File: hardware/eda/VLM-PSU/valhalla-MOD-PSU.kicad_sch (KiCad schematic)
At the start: 31 parts, among them J1 MAINS, J2 DC, J3 BUS, J4 GPIO, Q1 *3, U1 *2

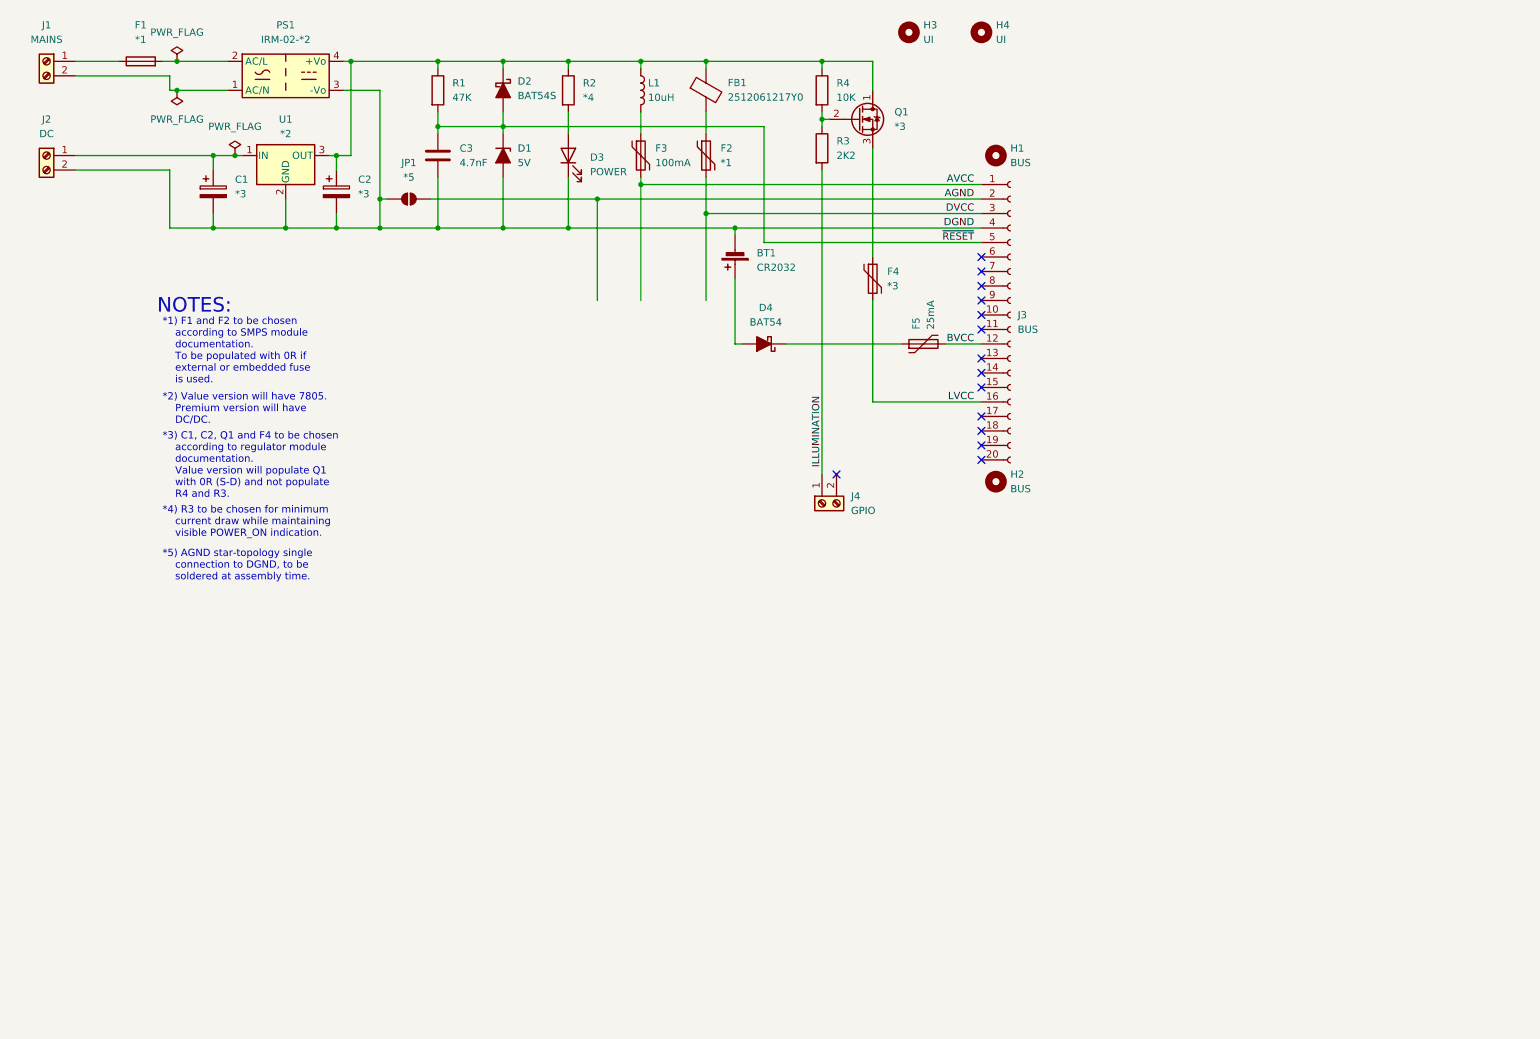
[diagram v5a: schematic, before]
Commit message: UPDATE: started work on MOD-PSU
  - adjusted schematic for cosmetics
  - changed power output to correct part to mate with Molex 5557
  - made /RESET generic (i.e. non-AVR targeted) and moved to a
    GPIO
    - upcoming CPU boards can elect whether to use the PSU-generated
      /RESET or come up with their own implementation
    - premium version will have a supervisor IC generating it,
      value version will have RC delay
  - opted to keep this MOD-PSU as is (i.e. MAINS or DC input) and
    develop a 2nd version for battery operation (UPS)
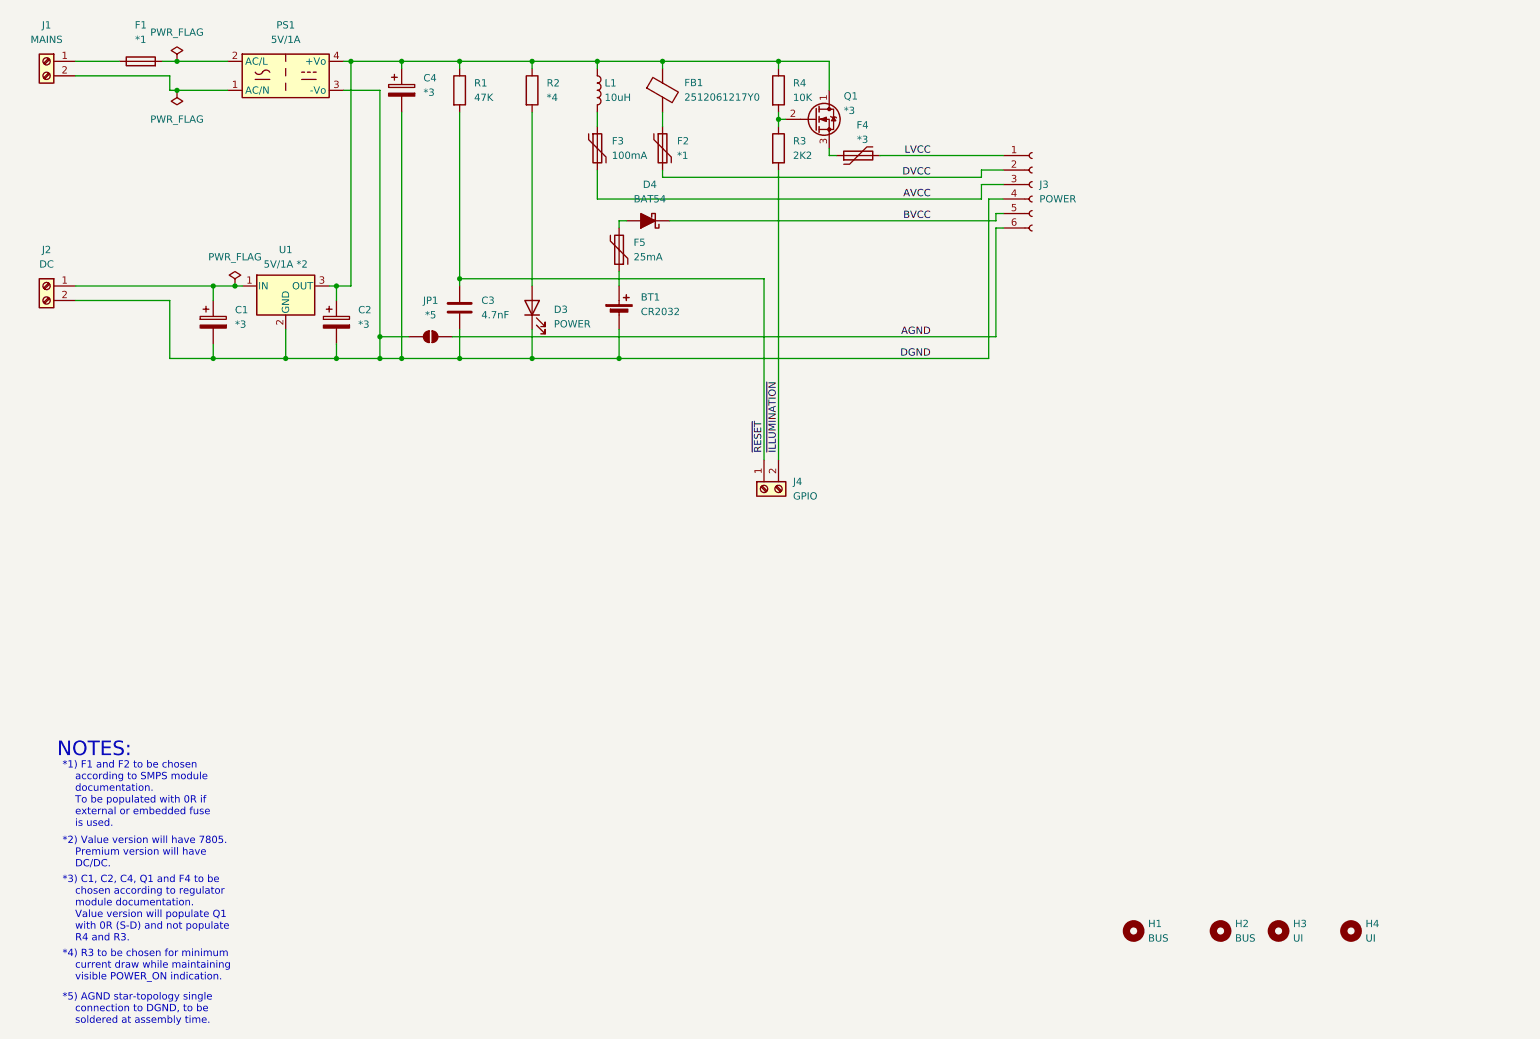
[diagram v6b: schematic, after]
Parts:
- removed D1: 5V, Diode_THT:D_DO-35_SOD27_P7.62mm_Horizontal, symbol Device:D_Zener_Filled
- removed D2: BAT54S, Diode_THT:D_DO-35_SOD27_P7.62mm_Horizontal, symbol Device:D_Schottky_Filled
- removed J3: BUS, Connector_PinSocket_2.54mm:PinSocket_2x10_P2.54mm_Vertical, symbol Connector:Conn_01x20_Socket
- added C4: *3, Capacitor_THT:CP_Radial_D5.0mm_P2.00mm, symbol Device:C_Polarized
- added J3: POWER, symbol Connector:Conn_01x06_Socket
- PS1: value IRM-02-*2 -> 5V/1A
- U1: value *2 -> 5V/1A *2
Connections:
- net AGND: now also J3.6 (Pin_6)
- net AVCC: now also J3.3 (Pin_3)
- net BVCC: now also D4.1 (K), J3.5 (Pin_5); no longer F5.2
- net DGND: now also C4.2, J3.4 (Pin_4)
- net DVCC: now also J3.2 (Pin_2)
- net LVCC: now also J3.1 (Pin_1)
- net ~{RESET}: now also J4.1 (Pin_1)
- net ~{ILLUMINATION}: now reaches J4.2 (Pin_2)
- net ~{ILLUMINATION}: now also R3.2
- net at F5.1: now also BT1.1 (+); no longer D4.1 (K)
- net at C2.1, FB1.1, L1.1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: now also C4.1
- net at D4.2 (A): now also F5.2; no longer BT1.1 (+)
- removed net ILLUMINATION: J4.1 (Pin_1), R3.2
- no-connect marks 14 -> 0
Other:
- note added: "*3) C1, C2, C4, Q1 and F4 to be chosen according to regulator module documentation. Value version will populate Q1 with 0R (S-D) and not populate R4 and R3."
- note removed: "*3) C1, C2, Q1 and F4 to be chosen according to regulator module documentation. Value version will populate Q1 with 0R (S-D) and not populate R4 and R3."
- moved on the sheet: BT1, C1, C2, C3, D3, D4, F2, F3, F4, F5, FB1, H1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

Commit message: UPDATE: progress on MOD-PSU
 - refined the schematic design and started work on the PCB layout
 - selected some critical components, resolved final footprints
   for others
 - found a good compromise for the (initially) /RESET line: using a
   supervisory circuit BUT using it as a POWER_GOOD output. A
   connected CPU can thus choose whether to interpret that as PG
   (early warning) or /RESET (closing shop).
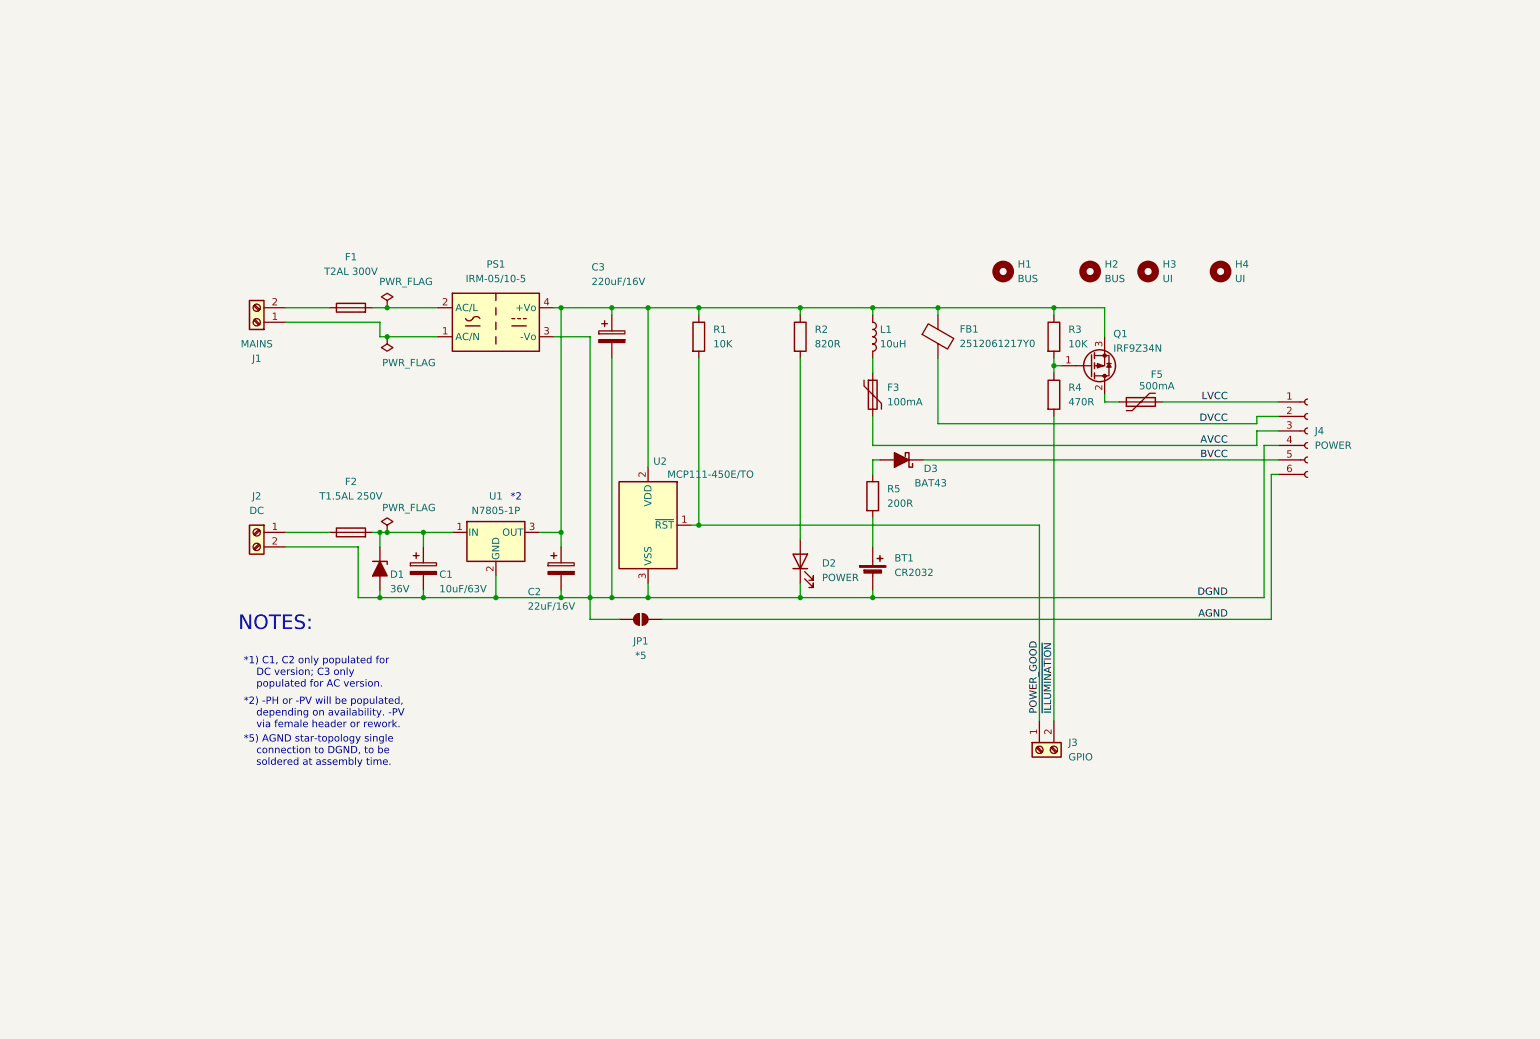
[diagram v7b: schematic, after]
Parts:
- removed C3: 4.7nF, Capacitor_THT:C_Rect_L7.0mm_W2.0mm_P5.00mm, symbol Device:C
- removed F2: *1, Fuse:Fuse_BelFuse_0ZRE0005FF_L8.3mm_W3.8mm, symbol Device:Polyfuse
- removed F4: *3, Fuse:Fuse_BelFuse_0ZRE0005FF_L8.3mm_W3.8mm, symbol Device:Polyfuse
- removed PS1: 5V/1A, Converter_ACDC:Converter_ACDC_MeanWell_IRM-02-xx_THT, symbol Converter_ACDC:IRM-02-3.3
- removed Q1: *3, Package_TO_SOT_THT:TO-92_Inline, symbol Transistor_FET:BS170
- added D1: 36V, Diode_THT:D_DO-41_SOD81_P5.08mm_Vertical_KathodeUp, symbol Device:D_Zener_Filled
- added F2: T1.5AL 250V, Fuse:Fuseholder_Clip-5x20mm_Bel_FC-203-22_Lateral_P17.80x5.00mm_D1.17mm_Horizontal, symbol Device:Fuse
- added PS1: IRM-05/10-5, Converter_ACDC:Converter_ACDC_MeanWell_IRM-05-xx_THT, symbol Converter_ACDC:IRM-05-5
- added Q1: IRF9Z34N, Package_TO_SOT_THT:TO-220-3_Horizontal_TabDown, symbol Transistor_FET:Q_PMOS_GDS
- added R5: 200R, Resistor_THT:R_Axial_DIN0207_L6.3mm_D2.5mm_P5.08mm_Vertical, symbol Device:R
- added U2: MCP111-450E/TO, Package_TO_SOT_THT:TO-92_Inline, symbol Power_Supervisor:MCP120-xxxDxTO
- BT1: footprint Battery:Battery_Panasonic_CR2032-VS1N_Vertical_CircularHoles -> Battery:Battery_Panasonic_CR2032-HFN_Horizontal_CircularHoles
- C1: value *3 -> 10uF/63V
- C2: value *3 -> 22uF/16V
- C3: renamed from C4; value *3 -> 220uF/16V; footprint Capacitor_THT:CP_Radial_D5.0mm_P2.00mm -> Capacitor_THT:CP_Radial_D6.3mm_P2.50mm
- D3: renamed from D4; value BAT54 -> BAT43; footprint Diode_THT:D_DO-35_SOD27_P7.62mm_Horizontal -> Diode_THT:D_DO-34_SOD68_P5.08mm_Vertical_KathodeUp
- F1: value *1 -> T2AL 300V; footprint Fuse:Fuseholder_Clip-5x20mm_Littelfuse_111_Lateral_P18.80x5.00mm_D1.17mm_Horizontal -> Fuse:Fuseholder_Clip-5x20mm_Bel_FC-203-22_Lateral_P17.80x5.00mm_D1.17mm_Horizontal
- F5: value 25mA -> 500mA
- J4: renamed from J3; footprint (none) -> PCM_EasyEDA:CONN-TN_39301060
- L1: footprint Inductor_THT:L_Radial_D7.0mm_P3.00mm -> Inductor_THT:L_Radial_D8.7mm_P5.00mm_Fastron_07HCP
- R1: value 47K -> 10K; footprint Resistor_THT:R_Axial_DIN0207_L6.3mm_D2.5mm_P7.62mm_Horizontal -> Resistor_THT:R_Axial_DIN0207_L6.3mm_D2.5mm_P5.08mm_Vertical
- R2: value *4 -> 820R; footprint Resistor_THT:R_Axial_DIN0207_L6.3mm_D2.5mm_P7.62mm_Horizontal -> Resistor_THT:R_Axial_DIN0207_L6.3mm_D2.5mm_P5.08mm_Vertical
- R3: renamed from R4; footprint Resistor_THT:R_Axial_DIN0207_L6.3mm_D2.5mm_P7.62mm_Horizontal -> Resistor_THT:R_Axial_DIN0207_L6.3mm_D2.5mm_P5.08mm_Vertical
- R4: renamed from R3; value 2K2 -> 470R; footprint Resistor_THT:R_Axial_DIN0207_L6.3mm_D2.5mm_P7.62mm_Horizontal -> Resistor_THT:R_Axial_DIN0207_L6.3mm_D2.5mm_P5.08mm_Vertical
- U1: value 5V/1A *2 -> N7805-1P
- renumbered D3 to D2, J4 to J3
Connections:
- net DGND: now also D1.2 (A), PS1.3 (-Vo), U2.3 (VSS)
- net DVCC: now also FB1.2
- net LVCC: now also F5.2
- net at F1.1: now also J1.2 (Pin_2); no longer J1.1 (Pin_1)
- net at F1.2: now also PS1.2 (AC/L)
- net at F5.1: now also Q1.2 (D); no longer BT1.1 (+)
- net at D3.2 (A): now also R5.1; no longer F5.2
- net at C2.1, C3.1, FB1.1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: now also PS1.4 (+Vo), Q1.3 (S), U2.2 (VDD)
- net at R3.2, R4.1: now also Q1.1 (G)
- net at C1.1, U1.1 (IN): now also D1.1 (K), F2.2; no longer J2.1 (Pin_1)
- net ~{RESET} renamed POWER_GOOD
- net POWER_GOOD: now also U2.1 (~{RST})
- new net: BT1.1 (+), R5.2
- new net: J1.1 (Pin_1), PS1.1 (AC/N)
- new net: F2.1, J2.1 (Pin_1)
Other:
- note added: "*1) C1, C2 only populated for DC version; C3 only populated for AC version."
- note added: "*2"
- note added: "*2) -PH or -PV will be populated, depending on availability. -PV via female header or rework."
- note removed: "*1) F1 and F2 to be chosen according to SMPS module documentation. To be populated with 0R if external or embedded fuse is used."
- note removed: "*2) Value version will have 7805. Premium version will have DC/DC."
- note removed: "*3) C1, C2, C4, Q1 and F4 to be chosen according to regulator module documentation. Value version will populate Q1 with 0R (S-D) and not populate R4 and R3."
- note removed: "*4) R3 to be chosen for minimum current draw while maintaining visible POWER_ON indication."
- moved on the sheet: BT1, C1, C2, C3, D2, D3, F1, F3, FB1, H1, H2, H3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
